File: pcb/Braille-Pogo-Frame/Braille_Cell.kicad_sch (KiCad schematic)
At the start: 1 part, among them J1 Conn_01x06

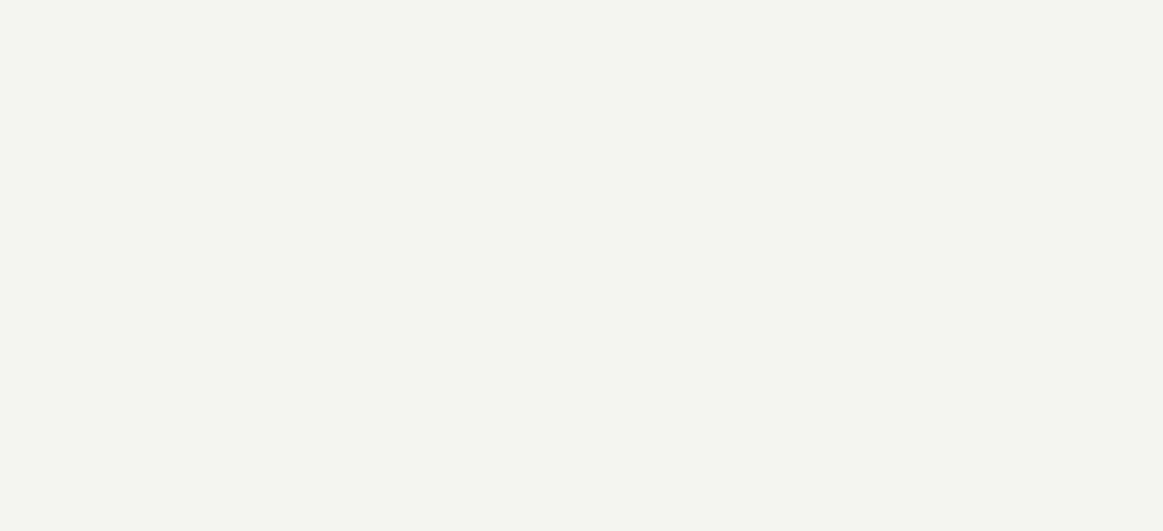
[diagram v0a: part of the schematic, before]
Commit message: Update microstepper pins
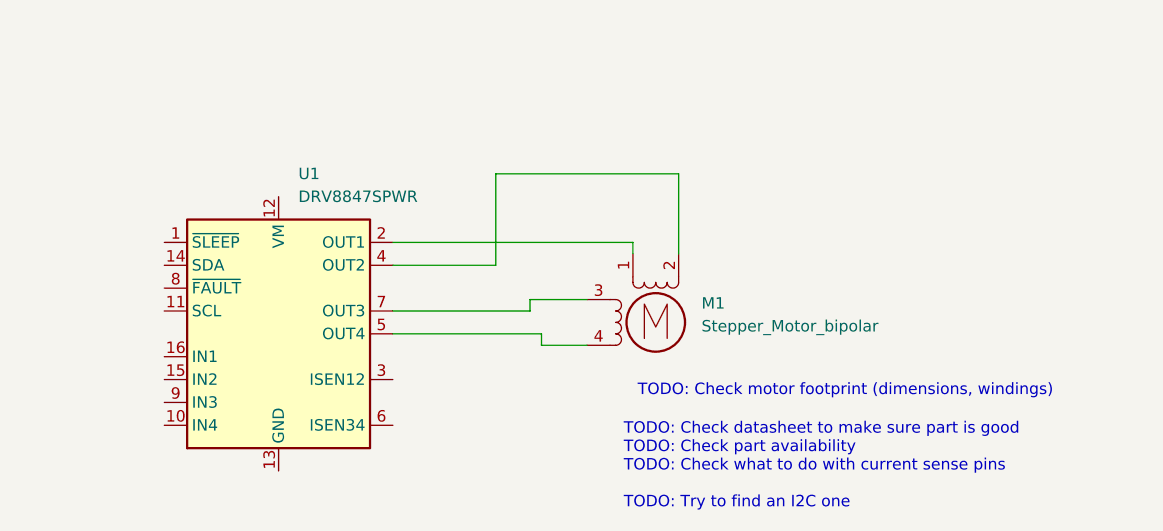
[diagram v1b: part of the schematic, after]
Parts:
- added M1: Stepper_Motor_bipolar, 00-lib-footprints:MicroStepper_8mm-2mmGear, symbol Motor:Stepper_Motor_bipolar
- added U1: DRV8847SPWR, Package_SO:TSSOP-16_4.4x5mm_P0.65mm, symbol Driver_Motor:DRV8847SPWR
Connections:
- new net: M1.1, U1.2 (OUT1)
- new net: M1.2 (-), U1.4 (OUT2)
- new net: M1.3, U1.7 (OUT3)
- new net: M1.4, U1.5 (OUT4)
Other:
- note added: "TODO: Check datasheet to make sure part is good TODO: Check part availability TODO: Check what to do with current sense pins TODO: Try to find an I2C one"
- note added: "TODO: Check motor footprint (dimensions, windings)"

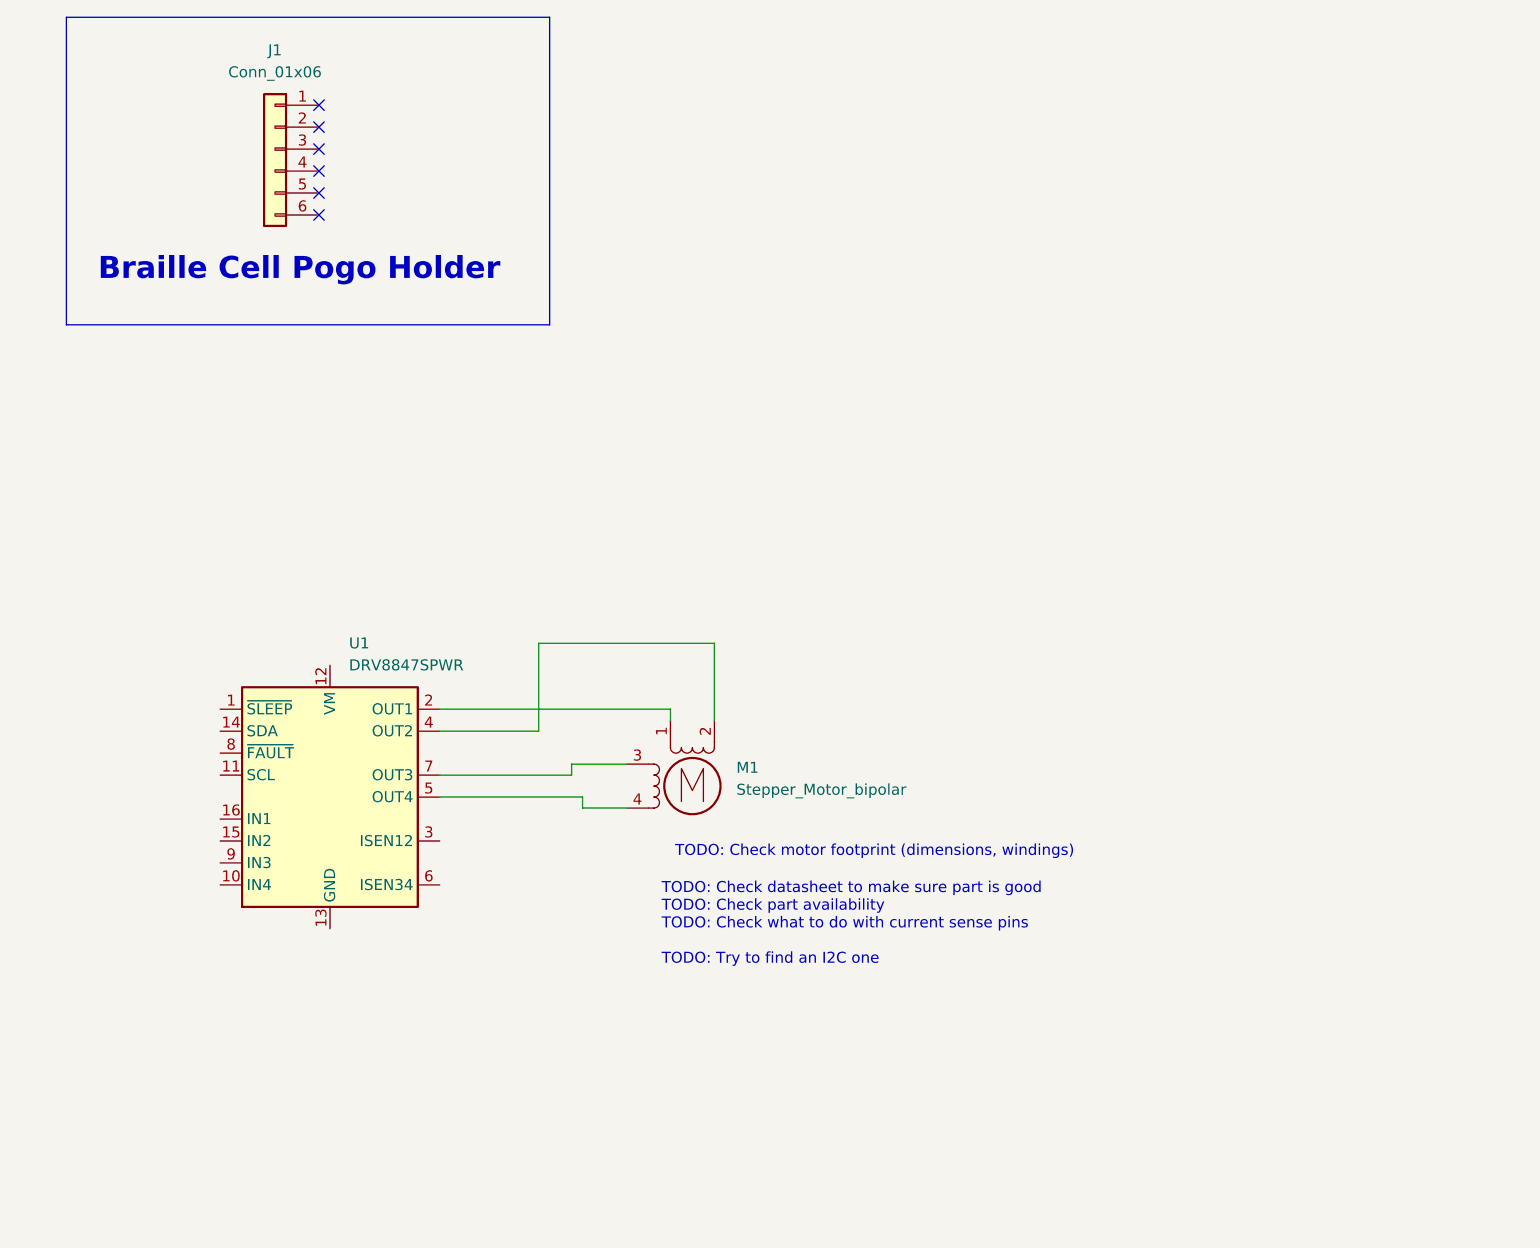
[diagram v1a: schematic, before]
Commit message: PCB: Add motors and motor driver to schematic
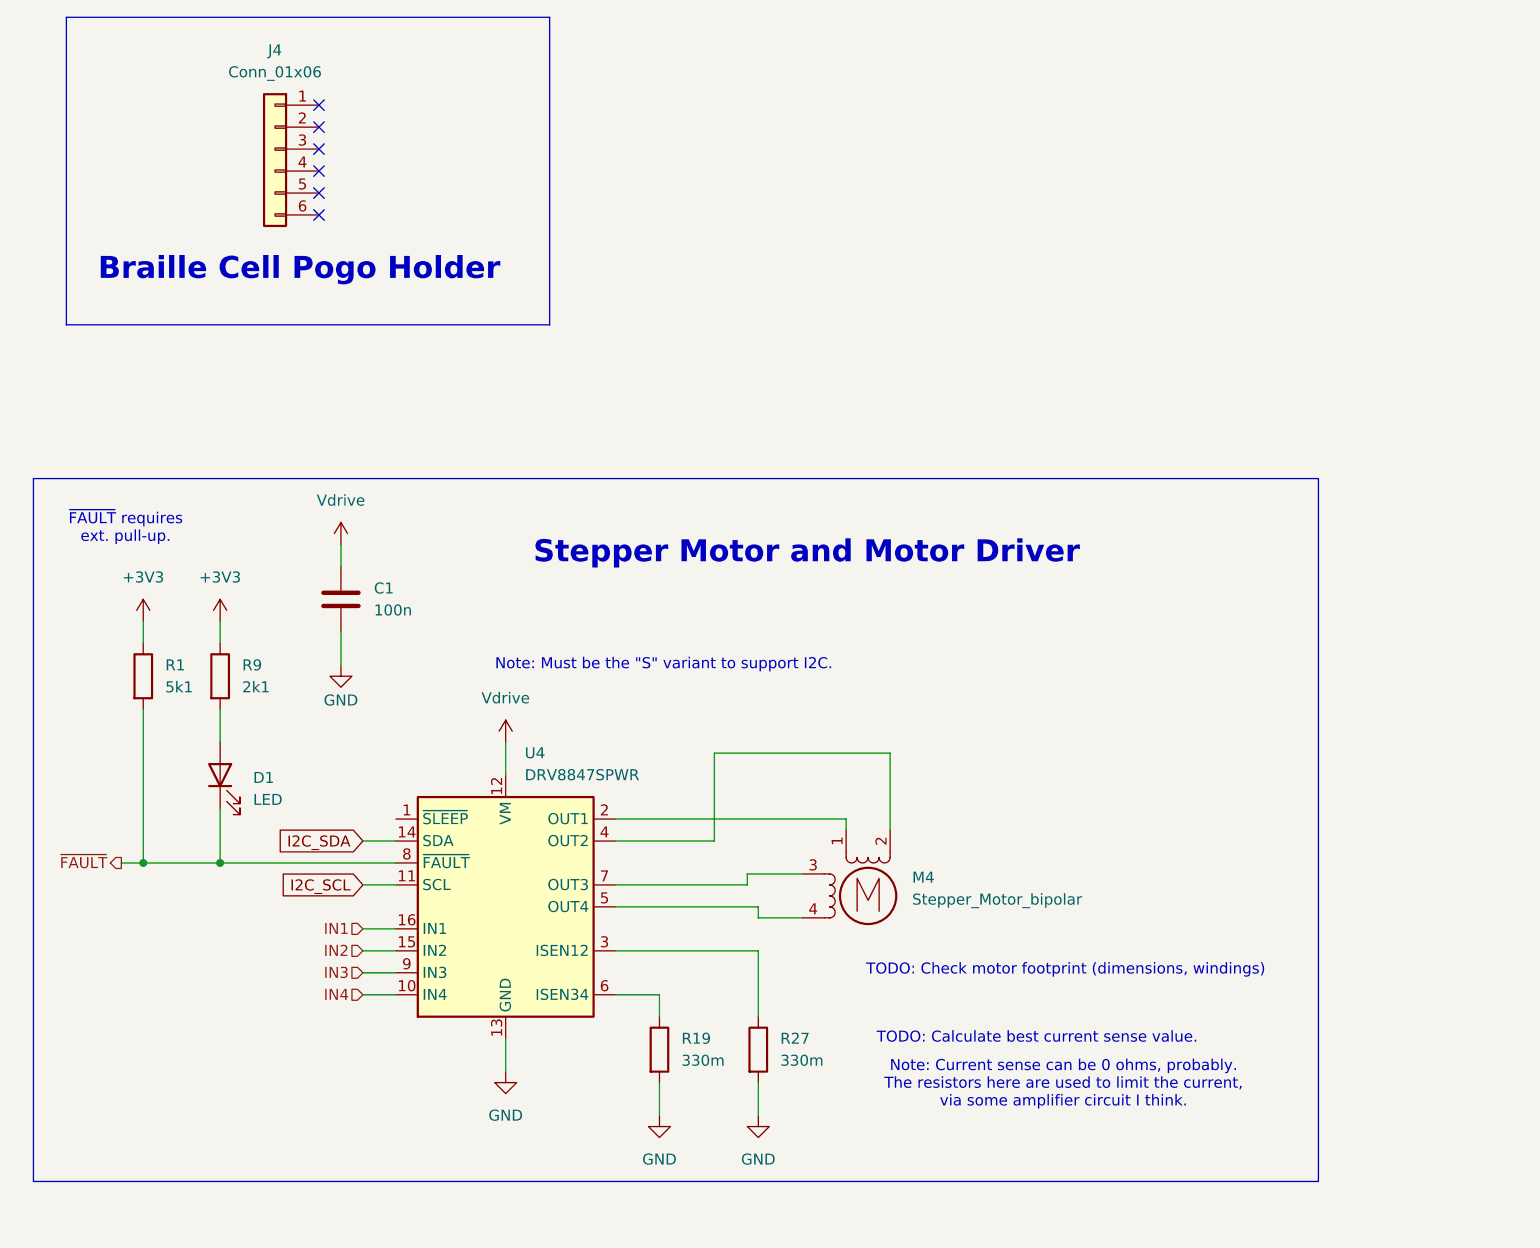
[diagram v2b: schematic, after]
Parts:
- added C1: 100n, symbol Device:C
- added D1: LED, symbol Device:LED
- added R1: 5k1, symbol Device:R
- added R19, R27: 330m, symbol Device:R
- added R9: 2k1, symbol Device:R
- renumbered J1 to J4, M1 to M4, U1 to U4
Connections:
- net IN4: now reaches U4.10 (IN4)
- net I2C_SCL: now reaches U4.11 (SCL)
- net Vdrive: now reaches U4.12 (VM)
- net Vdrive: now also C1.1
- net GND: now reaches U4.13 (GND)
- net GND: now also C1.2, R19.2, R27.2
- net I2C_SDA: now reaches U4.14 (SDA)
- net IN2: now reaches U4.15 (IN2)
- net IN1: now reaches U4.16 (IN1)
- net at U4.3 (ISEN12): now also R27.1
- net at U4.6 (ISEN34): now also R19.1
- net ~{FAULT}: now reaches U4.8 (~{FAULT})
- net ~{FAULT}: now also D1.1 (K), R1.2
- net IN3: now reaches U4.9 (IN3)
- new net: D1.2 (A), R9.2
- new net +3V3: R1.1, R9.1
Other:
- note added: "Note: Current sense can be 0 ohms, probably. The resistors here are used to limit the current, via some amplifier circuit I think."
- note added: "Note: Must be the "S" variant to support I2C."
- note added: "Stepper Motor and Motor Driver"
- note added: "TODO: Calculate best current sense value."
- note added: "~{FAULT} requires ext. pull-up."
- note removed: "TODO: Check datasheet to make sure part is good TODO: Check part availability TODO: Check what to do with current sense pins TODO: Try to find an I2C one"
- moved on the sheet: M4, U4

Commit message: PCB: Update footprint assignments
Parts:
- C1: footprint (none) -> Capacitor_SMD:C_1206_3216Metric_Pad1.33x1.80mm_HandSolder
- D1: footprint (none) -> LED_SMD:LED_1206_3216Metric_Pad1.42x1.75mm_HandSolder
- R1, R19, R27, R9: footprint (none) -> Resistor_SMD:R_1206_3216Metric_Pad1.30x1.75mm_HandSolder
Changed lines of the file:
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@@
 			)
 		)
-		(property "Footprint" ""
+		(property "Footprint" "Resistor_SMD:R_1206_3216Metric_Pad1.30x1.75mm_HandSolder"
 			(at 50.292 101.6 90)
 			(effects
@@
 			)
 		)
-		(property "Footprint" ""
+		(property "Footprint" "LED_SMD:LED_1206_3216Metric_Pad1.42x1.75mm_HandSolder"
 			(at 52.07 113.03 0)
 			(effects
@@
 			)
 		)
-		(property "Footprint" ""
+		(property "Footprint" "Resistor_SMD:R_1206_3216Metric_Pad1.30x1.75mm_HandSolder"
 			(at 41.402 101.6 90)
 			(effects
@@
 			)
 		)
-		(property "Footprint" ""
+		(property "Footprint" "Resistor_SMD:R_1206_3216Metric_Pad1.30x1.75mm_HandSolder"
 			(at 101.092 144.78 90)
 			(effects
@@
 			)
 		)
-		(property "Footprint" ""
+		(property "Footprint" "Capacitor_SMD:C_1206_3216Metric_Pad1.33x1.80mm_HandSolder"
 			(at 67.0052 96.52 0)
 			(effects
@@
 			)
 		)
-		(property "Footprint" ""
+		(property "Footprint" "Resistor_SMD:R_1206_3216Metric_Pad1.30x1.75mm_HandSolder"
 			(at 112.522 144.78 90)
 			(effects

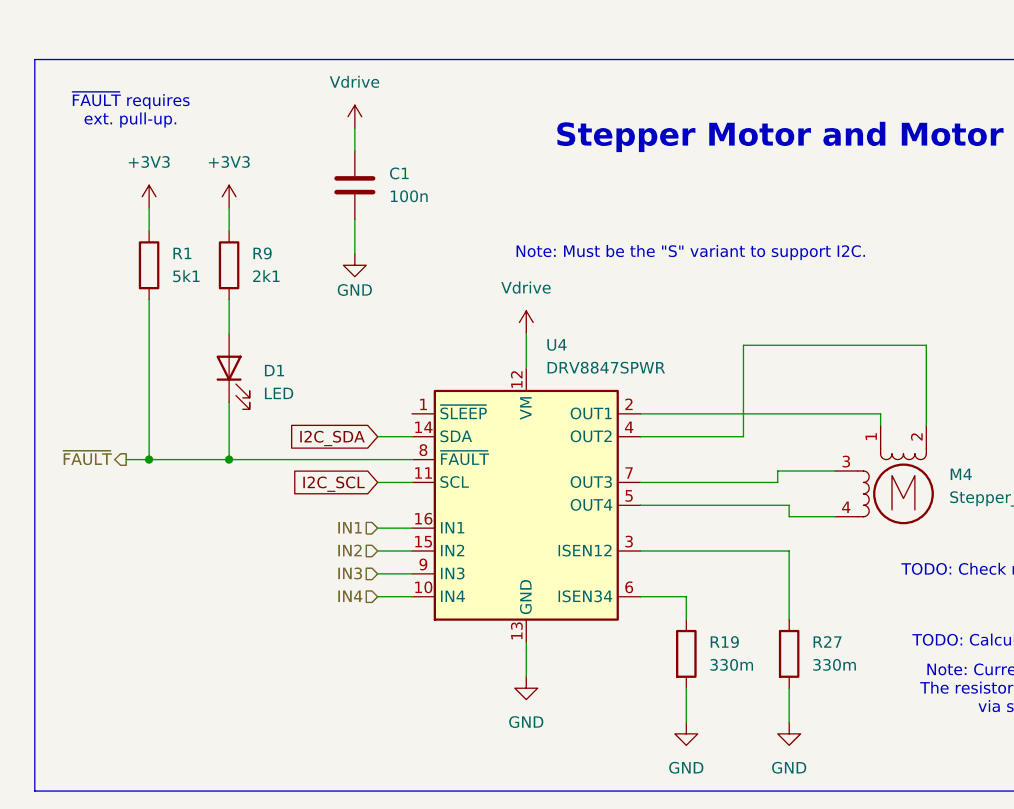
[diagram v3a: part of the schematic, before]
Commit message: PCB: Place motor drivers and horiz. rail mounts
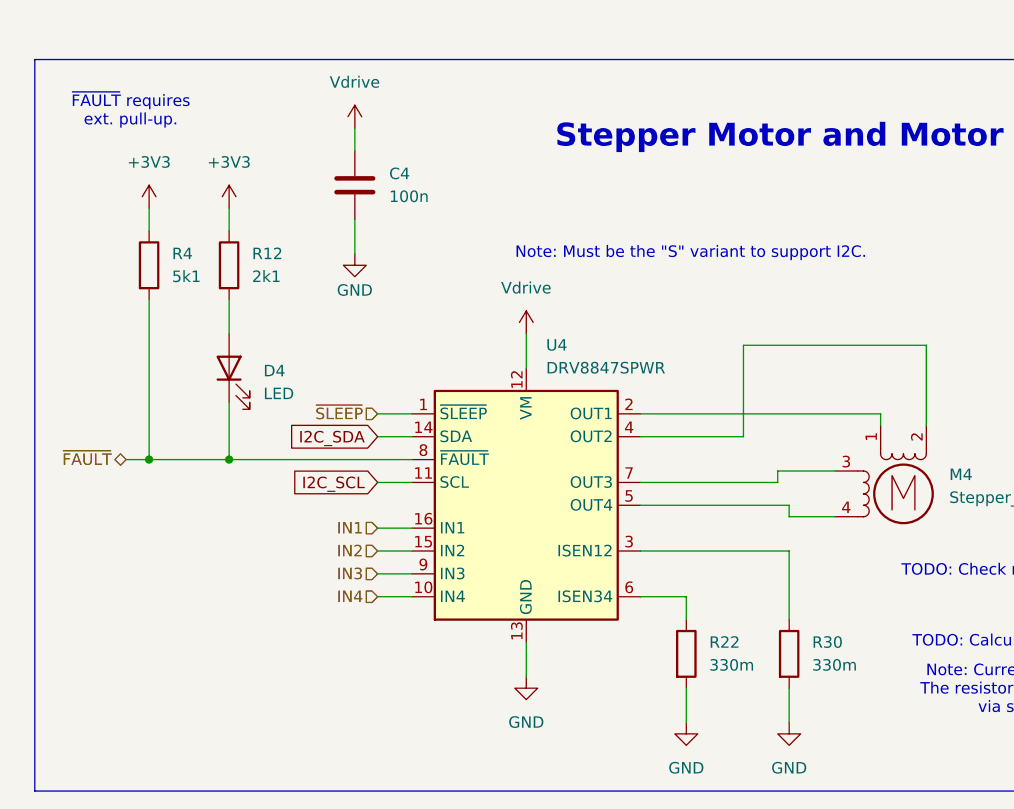
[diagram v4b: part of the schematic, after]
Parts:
- renumbered C1 to C4, D1 to D4, R9 to R12, R19 to R22, R27 to R30, R1 to R4
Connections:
- net ~{SLEEP}: now reaches U4.1 (~{SLEEP})

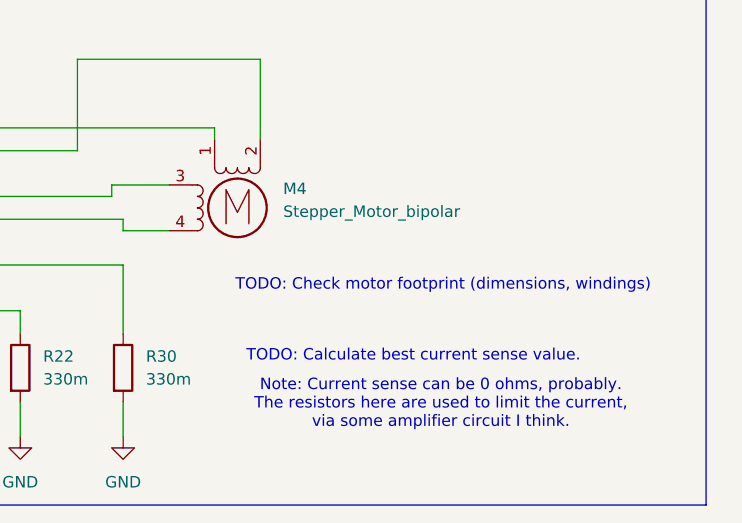
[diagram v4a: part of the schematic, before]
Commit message: Update stepper motor cad dimensions, PCB footprint mostly
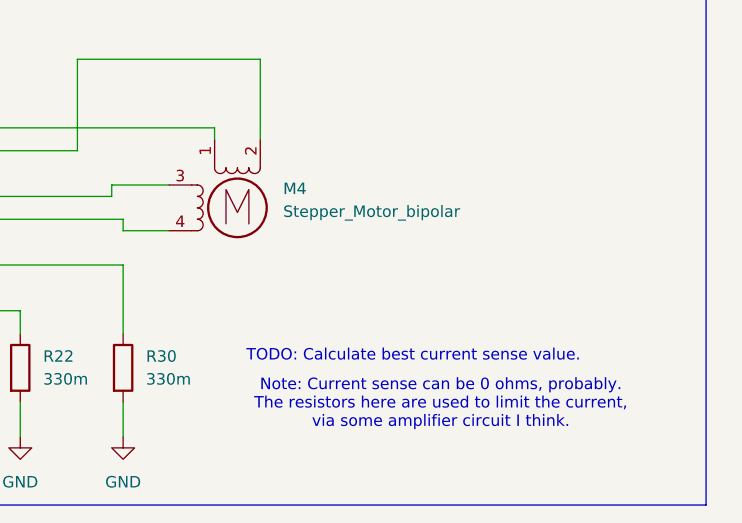
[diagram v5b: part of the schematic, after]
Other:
- note removed: "TODO: Check motor footprint (dimensions, windings)"
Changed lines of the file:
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@@
-		)
-	)
-	(text "TODO: Check motor footprint (dimensions, windings)"
-		(exclude_from_sim no)
-		(at 149.86 135.636 0)
-		(effects
-			(font
-				(size 1.27 1.27)
-			)
 		)
 	)
